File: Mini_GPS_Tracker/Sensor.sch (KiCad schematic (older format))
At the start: 13 parts, among them U2 MS5611-01BA, U7 LSM9DS1

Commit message: added stm chip
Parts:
- gave numbers to parts that had none: 5
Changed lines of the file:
@@
 $EndComp
 $Comp
-L Sensor_Motion:BNO055 U?
+L Sensor_Motion:BNO055 U12
 U 1 1 5E8555C8
 P 8300 4850
-F 0 "U?" H 8300 5731 50  0000 C CNN
+F 0 "U12" H 8300 5731 50  0000 C CNN
 F 1 "BNO055" H 8300 5640 50  0000 C CNN
 F 2 "Package_LGA:LGA-28_5.2x3.8mm_P0.5mm" H 8550 4200 50  0001 L CNN
@@
 $EndComp
 $Comp
-L Sensor_Motion:ADXL343 U?
+L Sensor_Motion:ADXL343 U11
 U 1 1 5E8940BD
 P 5450 2300
-F 0 "U?" H 5994 2346 50  0000 L CNN
+F 0 "U11" H 5994 2346 50  0000 L CNN
 F 1 "ADXL343" H 5994 2255 50  0000 L CNN
 F 2 "Package_LGA:LGA-14_3x5mm_P0.8mm_LayoutBorder1x6y" H 5450 2300 50  0001 C CNN
@@
 $EndComp
 $Comp
-L power:GND #PWR?
+L power:GND #PWR0119
 U 1 1 5E8951BC
 P 5450 3300
-F 0 "#PWR?" H 5450 3050 50  0001 C CNN
+F 0 "#PWR0119" H 5450 3050 50  0001 C CNN
 F 1 "GND" H 5455 3127 50  0000 C CNN
 F 2 "" H 5450 3300 50  0001 C CNN
@@
 	4400 2200 4950 2200
 $Comp
-L pspice:CAP C?
+L pspice:CAP C21
 U 1 1 5E89F2A3
 P 6650 2300
-F 0 "C?" H 6828 2346 50  0000 L CNN
+F 0 "C21" H 6828 2346 50  0000 L CNN
 F 1 "0.1uF" H 6828 2255 50  0000 L CNN
 F 2 "" H 6650 2300 50  0001 C CNN
@@
 $EndComp
 $Comp
-L pspice:CAP C?
+L pspice:CAP C22
 U 1 1 5E89F917
 P 7150 2300
-F 0 "C?" H 7328 2346 50  0000 L CNN
+F 0 "C22" H 7328 2346 50  0000 L CNN
 F 1 "0.1uF" H 7328 2255 50  0000 L CNN
 F 2 "" H 7150 2300 50  0001 C CNN
@@
 	5450 2900 5450 3150
 $Comp
-L pspice:CAP C?
+L pspice:CAP C23
 U 1 1 5E8A3F23
 P 7650 2300
-F 0 "C?" H 7828 2346 50  0000 L CNN
+F 0 "C23" H 7828 2346 50  0000 L CNN
 F 1 "10uF" H 7828 2255 50  0000 L CNN
 F 2 "" H 7650 2300 50  0001 C CNN

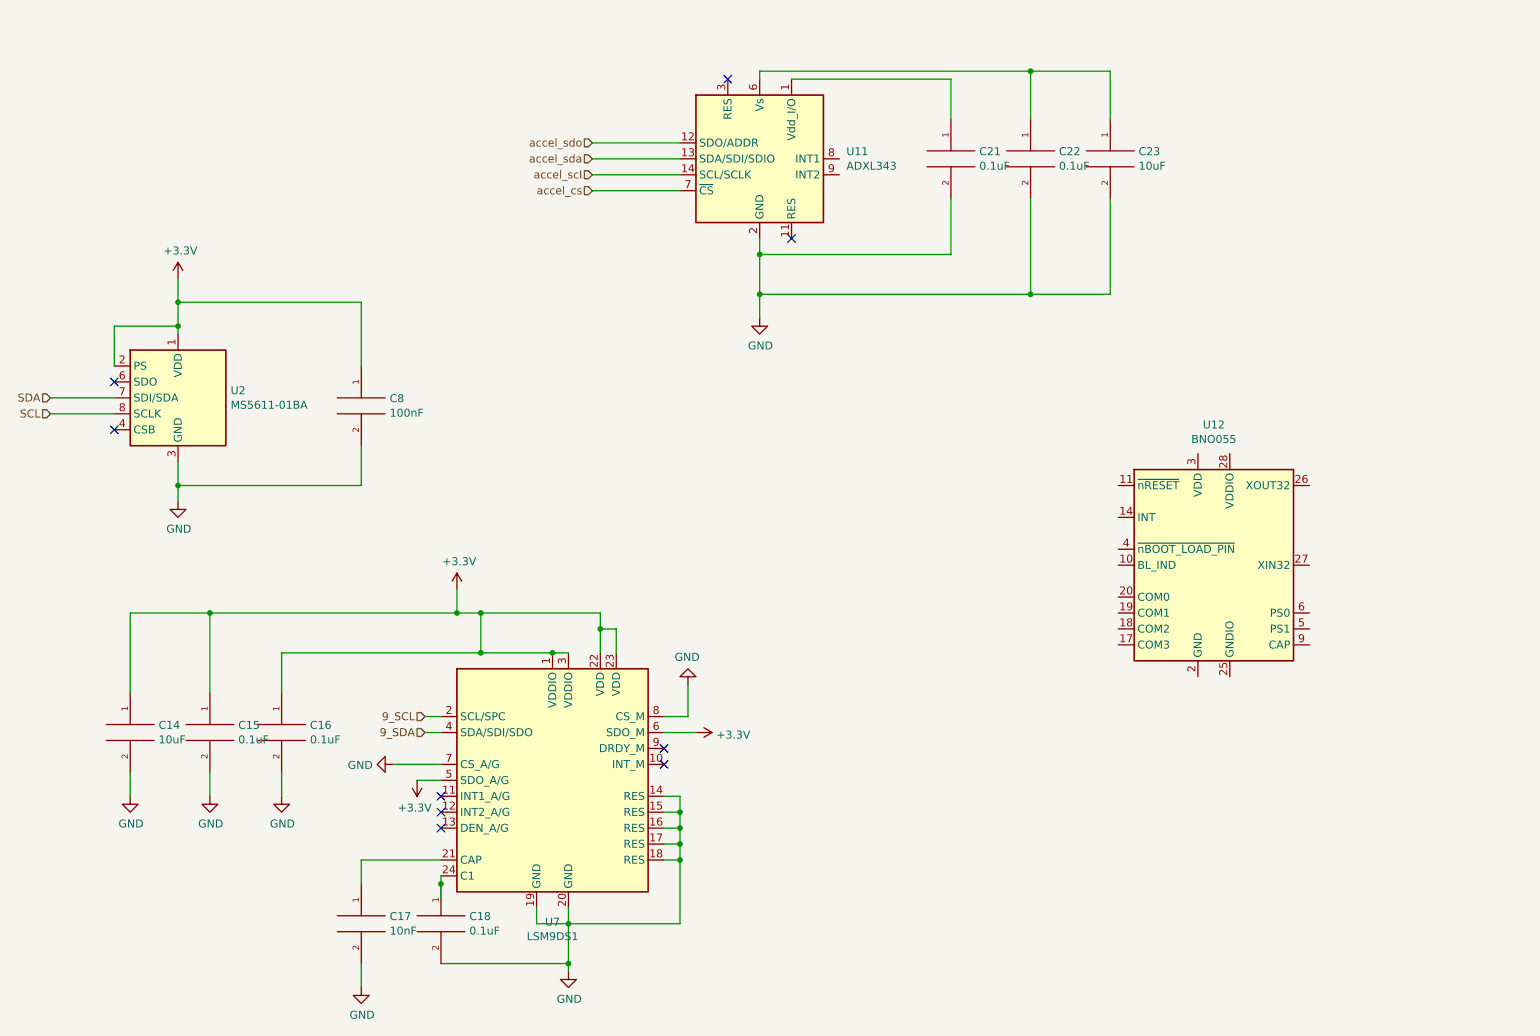
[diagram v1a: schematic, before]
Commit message: added bluetooth wifi module
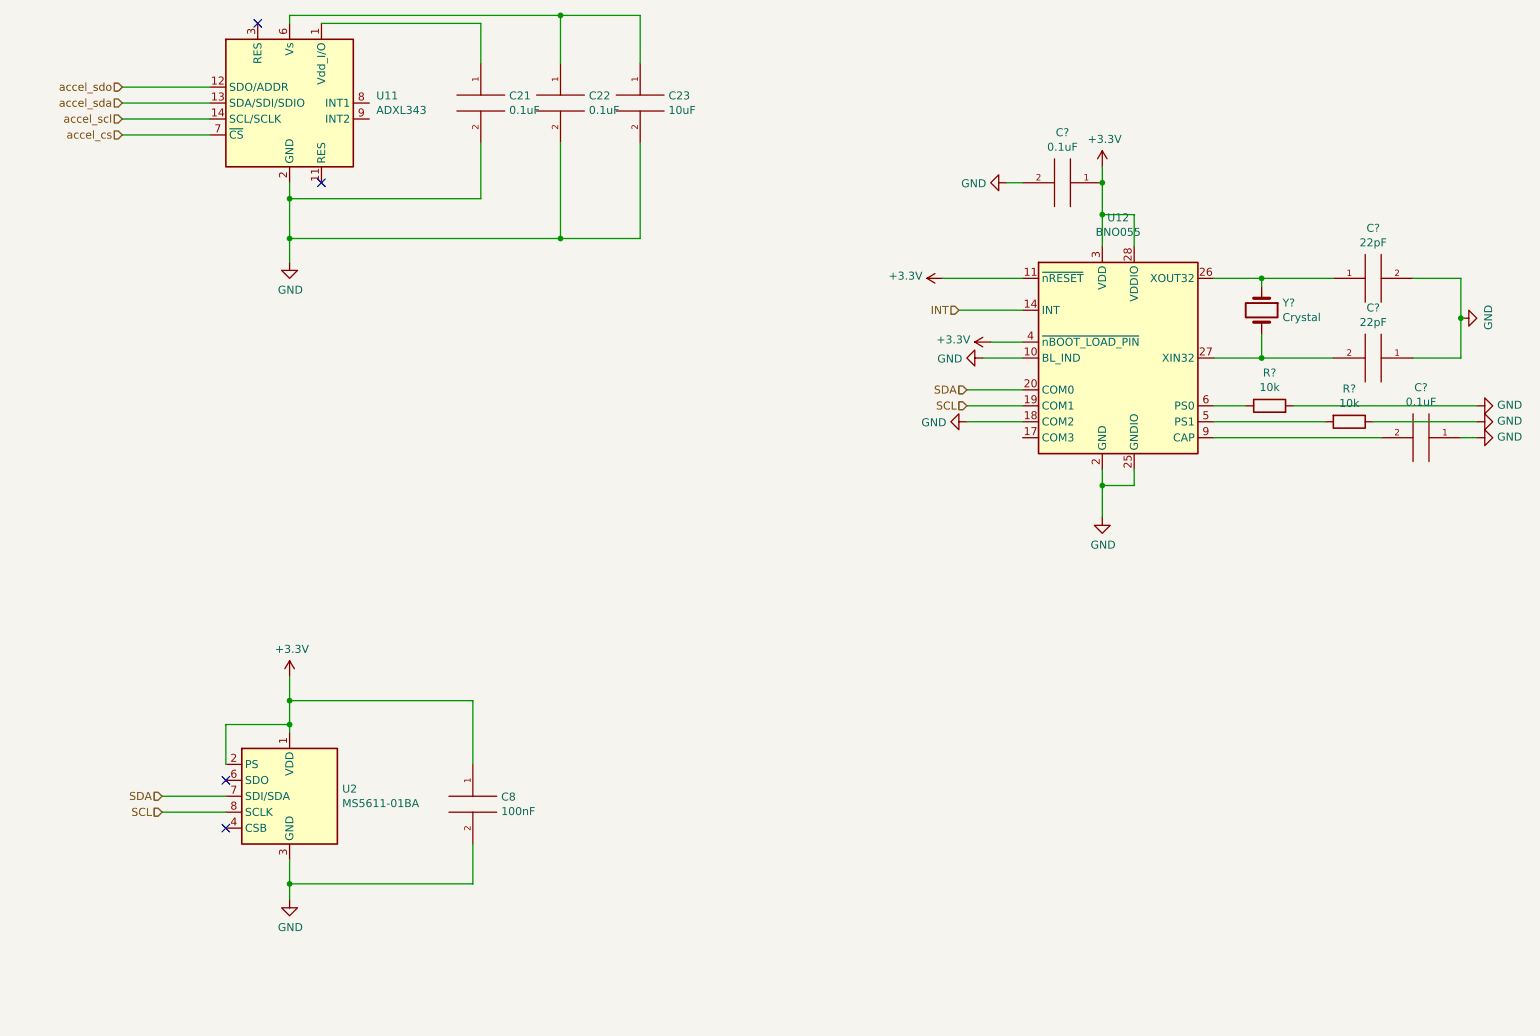
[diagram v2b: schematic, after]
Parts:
- removed C14: 10uF, Capacitor_SMD:C_0805_2012Metric_Pad1.15x1.40mm_HandSolder, symbol pspice:CAP
- removed C15, C16, C18: 0.1uF, Capacitor_SMD:C_0805_2012Metric_Pad1.15x1.40mm_HandSolder, symbol pspice:CAP
- removed C17: 10nF, Capacitor_SMD:C_0805_2012Metric_Pad1.15x1.40mm_HandSolder, symbol pspice:CAP
- removed U7: LSM9DS1, Package_LGA:LGA-24L_3x3.5mm_P0.43mm, symbol Sensor_Motion:LSM9DS1
- added C? (x2): 22pF, symbol pspice:CAP
- added C? (x2): 0.1uF, symbol pspice:CAP
- added R? (x2): 10k, symbol Device:R
- added Y?: Crystal, symbol Device:Crystal
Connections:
- net +3V3: now also U12.11 (~nRESET), U12.28 (VDDIO), U12.3 (VDD), U12.4 (~nBOOT_LOAD_PIN), C?.1
- net GND: now also U12.10 (BL_IND), U12.15 (GNDIO), U12.16 (GNDIO), U12.18 (COM2), U12.2 (GND), U12.25 (GNDIO), C?.1, C?.1, C?.2, C?.2, R?.1, R?.2
- net SCL: now also U12.19 (COM1)
- net SDA: now also U12.20 (COM0)
- net INT: now reaches U12.14 (INT)
- net at U12.26 (XOUT32): now also C?.1, Y?.1
- net at U12.27 (XIN32): now also C?.2, Y?.2
- net at U12.5 (PS1): now also R?.2
- net at U12.6 (PS0): now also R?.1
- net at U12.9 (CAP): now also C?.2
- no-connect marks 9 -> 4
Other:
- moved on the sheet: C21, C22, C23, C8, U11, U12, U2

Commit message: added motion
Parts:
- added R?: 10K, symbol Device:R
- Y?: value Crystal -> 32.7568KHz
- renumbered C8 to C?, C21 to C?, C22 to C?, C23 to C?, U2 to U?, U12 to U?, U11 to U?
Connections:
- net +3V3: no longer U?.11 (~nRESET)
- net GND: now also C?.2, R?.2; no longer C?.1
- net SCL: no longer U?.19 (COM1)
- net SDA: no longer U?.20 (COM0)
- net at U?.17 (COM3): now also R?.1
- net at U?.9 (CAP): now also C?.1; no longer C?.2
- net INT renamed BNO055_INTERRUPT
- new net BNO055_RESET: U?.11 (~nRESET)
- new net BNO055_SCL: U?.19 (COM1)
- new net BNO055_SDA: U?.20 (COM0)
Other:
- moved on the sheet: C?
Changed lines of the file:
@@
 $EndDescr
 $Comp
-L Sensor_Motion:BNO055 U12
+L Sensor_Motion:BNO055 U?
 U 1 1 5E8555C8
 P 7700 3550
-F 0 "U12" H 7700 4431 50  0000 C CNN
+F 0 "U?" H 7700 4431 50  0000 C CNN
 F 1 "BNO055" H 7700 4340 50  0000 C CNN
 F 2 "Package_LGA:LGA-28_5.2x3.8mm_P0.5mm" H 7950 2900 50  0001 L CNN
@@
 	2500 6700 2500 6850
 $Comp
-L pspice:CAP C8
+L pspice:CAP C?
 U 1 1 5E6E943F
 P 3650 6350
-F 0 "C8" H 3828 6396 50  0000 L CNN
+F 0 "C?" H 3828 6396 50  0000 L CNN
 F 1 "100nF" H 3828 6305 50  0000 L CNN
 F 2 "Capacitor_SMD:C_0805_2012Metric_Pad1.15x1.40mm_HandSolder" H 3650 6350 50  0001 C CNN
@@
 $EndComp
 $Comp
-L power:+3.3V #PWR016
+L power:+3.3V #PWR?
 U 1 1 5E6E8AC2
 P 2500 5550
-F 0 "#PWR016" H 2500 5400 50  0001 C CNN
+F 0 "#PWR?" H 2500 5400 50  0001 C CNN
 F 1 "+3.3V" H 2515 5723 50  0000 C CNN
 F 2 "" H 2500 5550 50  0001 C CNN
@@
 $EndComp
 $Comp
-L power:GND #PWR017
+L power:GND #PWR?
 U 1 1 5E6E7BFC
 P 2500 6950
-F 0 "#PWR017" H 2500 6700 50  0001 C CNN
+F 0 "#PWR?" H 2500 6700 50  0001 C CNN
 F 1 "GND" H 2505 6777 50  0000 C CNN
 F 2 "" H 2500 6950 50  0001 C CNN
@@
 	1700 6400 2100 6400
 $Comp
-L Sensor_Pressure:MS5611-01BA U2
+L Sensor_Pressure:MS5611-01BA U?
 U 1 1 5E6E6D79
 P 2500 6300
-F 0 "U2" H 2830 6346 50  0000 L CNN
+F 0 "U?" H 2830 6346 50  0000 L CNN
 F 1 "MS5611-01BA" H 2830 6255 50  0000 L CNN
 F 2 "Package_LGA:LGA-8_3x5mm_P1.25mm" H 2500 6300 50  0001 C CNN
@@
 $EndComp
 $Comp
-L Sensor_Motion:ADXL343 U11
+L Sensor_Motion:ADXL343 U?
 U 1 1 5E8940BD
 P 2500 1950
-F 0 "U11" H 3044 1996 50  0000 L CNN
+F 0 "U?" H 3044 1996 50  0000 L CNN
 F 1 "ADXL343" H 3044 1905 50  0000 L CNN
 F 2 "Package_LGA:LGA-14_3x5mm_P0.8mm_LayoutBorder1x6y" H 2500 1950 50  0001 C CNN
@@
 $EndComp
 $Comp
-L power:GND #PWR0119
+L power:GND #PWR?
 U 1 1 5E8951BC
 P 2500 2950
-F 0 "#PWR0119" H 2500 2700 50  0001 C CNN
+F 0 "#PWR?" H 2500 2700 50  0001 C CNN
 F 1 "GND" H 2505 2777 50  0000 C CNN
 F 2 "" H 2500 2950 50  0001 C CNN
@@
 	1450 1850 2000 1850
 $Comp
-L pspice:CAP C21
+L pspice:CAP C?
 U 1 1 5E89F2A3
 P 3700 1950
-F 0 "C21" H 3878 1996 50  0000 L CNN
+F 0 "C?" H 3878 1996 50  0000 L CNN
 F 1 "0.1uF" H 3878 1905 50  0000 L CNN
 F 2 "" H 3700 1950 50  0001 C CNN
@@
 $EndComp
 $Comp
-L pspice:CAP C22
+L pspice:CAP C?
 U 1 1 5E89F917
 P 4200 1950
-F 0 "C22" H 4378 1996 50  0000 L CNN
+F 0 "C?" H 4378 1996 50  0000 L CNN
 F 1 "0.1uF" H 4378 1905 50  0000 L CNN
 F 2 "" H 4200 1950 50  0001 C CNN
@@
 	2500 2550 2500 2800
 $Comp
-L pspice:CAP C23
+L pspice:CAP C?
 U 1 1 5E8A3F23
 P 4700 1950
-F 0 "C23" H 4878 1996 50  0000 L CNN
+F 0 "C?" H 4878 1996 50  0000 L CNN
 F 1 "10uF" H 4878 1905 50  0000 L CNN
 F 2 "" H 4700 1950 50  0001 C CNN
@@
 P 8600 3250
 F 0 "Y?" V 8554 3381 50  0000 L CNN
-F 1 "Crystal" V 8645 3381 50  0000 L CNN
+F 1 "32.7568KHz" V 8645 3381 50  0000 L CNN
 F 2 "" H 8600 3250 50  0001 C CNN
 F 3 "~" H 8600 3250 50  0001 C CNN
@@
 Wire Wire Line
 	8600 3050 9050 3050
-$Comp
-L power:+3.3V #PWR?
-U 1 1 5E88C4D2
-P 6900 3450
-F 0 "#PWR?" H 6900 3300 50  0001 C CNN
-F 1 "+3.3V" V 6915 3578 50  0000 L CNN
-F 2 "" H 6900 3450 50  0001 C CNN
-F 3 "" H 6900 3450 50  0001 C CNN
-	1    6900 3450
-	0    -1   -1   0
-$EndComp
-Wire Wire Line
-	6900 3450 7100 3450
 $Comp
 L power:GND #PWR?
@@
 L pspice:CAP C?
 U 1 1 5E8959B0
-P 9600 4050
-F 0 "C?" V 9285 4050 50  0000 C CNN
-F 1 "0.1uF" V 9376 4050 50  0000 C CNN
-F 2 "" H 9600 4050 50  0001 C CNN
-F 3 "~" H 9600 4050 50  0001 C CNN
-	1    9600 4050
-	0    1    1    0
+P 8550 4450
+F 0 "C?" V 8235 4450 50  0000 C CNN
+F 1 "0.1uF" V 8326 4450 50  0000 C CNN
+F 2 "" H 8550 4450 50  0001 C CNN
+F 3 "~" H 8550 4450 50  0001 C CNN
+	1    8550 4450
+	1    0    0    -1
 $EndComp
 $Comp
 L power:GND #PWR?
 U 1 1 5E89C6D8
-P 9950 4050
-F 0 "#PWR?" H 9950 3800 50  0001 C CNN
-F 1 "GND" V 9955 3922 50  0000 R CNN
-F 2 "" H 9950 4050 50  0001 C CNN
-F 3 "" H 9950 4050 50  0001 C CNN
-	1    9950 4050
-	0    -1   -1   0
+P 8550 4800
+F 0 "#PWR?" H 8550 4550 50  0001 C CNN
+F 1 "GND" V 8555 4672 50  0000 R CNN
+F 2 "" H 8550 4800 50  0001 C CNN
+F 3 "" H 8550 4800 50  0001 C CNN
+	1    8550 4800
+	1    0    0    -1
 $EndComp
 Wire Wire Line
@@
 	8300 3950 9000 3950
 Wire Wire Line
-	8300 4050 9350 4050
-Wire Wire Line
-	9850 4050 9950 4050
+	8550 4700 8550 4800
 Wire Wire Line
 	9300 3950 9950 3950
-$Comp
-L power:+3.3V #PWR?
-U 1 1 5E8A2C38
-P 6600 3050
-F 0 "#PWR?" H 6600 2900 50  0001 C CNN
-F 1 "+3.3V" V 6615 3178 50  0000 L CNN
-F 2 "" H 6600 3050 50  0001 C CNN
-F 3 "" H 6600 3050 50  0001 C CNN
-	1    6600 3050
-	0    -1   -1   0
-$EndComp
-Wire Wire Line
-	6600 3050 7100 3050
-Text HLabel 6750 3750 0    50   Input ~ 0
-SDA
-Text HLabel 6750 3850 0    50   Input ~ 0
-SCL
-Wire Wire Line
-	6750 3750 7100 3750
-Wire Wire Line
-	6750 3850 7100 3850
-$Comp
-L power:GND #PWR?
-U 1 1 5E8A7FB3
-P 6750 3950
-F 0 "#PWR?" H 6750 3700 50  0001 C CNN
-F 1 "GND" V 6755 3822 50  0000 R CNN
-F 2 "" H 6750 3950 50  0001 C CNN
-F 3 "" H 6750 3950 50  0001 C CNN
-	1    6750 3950
-	0    1    1    0
-$EndComp
-Wire Wire Line
-	6750 3950 7100 3950
 Wire Wire Line
 	7800 4250 7800 4350
@@
 Wire Wire Line
 	7600 4350 7600 4550
-$Comp
-L power:GND #PWR?
-U 1 1 5E8AC9F0
-P 6850 3550
-F 0 "#PWR?" H 6850 3300 50  0001 C CNN
-F 1 "GND" V 6855 3422 50  0000 R CNN
-F 2 "" H 6850 3550 50  0001 C CNN
-F 3 "" H 6850 3550 50  0001 C CNN
-	1    6850 3550
-	0    1    1    0
-$EndComp
-Wire Wire Line
-	6850 3550 7100 3550
-Text HLabel 6700 3250 0    50   Input ~ 0
-INT
-Wire Wire Line
-	6700 3250 7100 3250
+Wire Wire Line
+	8300 4050 8550 4050
+Wire Wire Line
+	8550 4050 8550 4200
+$Comp
+L Device:R R?
+U 1 1 5E897EFC
+P 6950 4300
+F 0 "R?" H 7020 4346 50  0000 L CNN
+F 1 "10K" H 7020 4255 50  0000 L CNN
+F 2 "" V 6880 4300 50  0001 C CNN
+F 3 "~" H 6950 4300 50  0001 C CNN
+	1    6950 4300
+	1    0    0    -1
+$EndComp
+$Comp
+L power:GND #PWR?
+U 1 1 5E898E99
+P 6950 4550
+F 0 "#PWR?" H 6950 4300 50  0001 C CNN
+F 1 "GND" H 6955 4377 50  0000 C CNN
+F 2 "" H 6950 4550 50  0001 C CNN
+F 3 "" H 6950 4550 50  0001 C CNN
+	1    6950 4550
+	1    0    0    -1
+$EndComp
+$Comp
+L power:GND #PWR?
+U 1 1 5E89968D
+P 6600 4550
+F 0 "#PWR?" H 6600 4300 50  0001 C CNN
+F 1 "GND" H 6605 4377 50  0000 C CNN
+F 2 "" H 6600 4550 50  0001 C CNN
+F 3 "" H 6600 4550 50  0001 C CNN
+	1    6600 4550
+	1    0    0    -1
+$EndComp
+Wire Wire Line
+	6950 4550 6950 4450
+Wire Wire Line
+	6950 4150 6950 4050
+Wire Wire Line
+	6950 4050 7100 4050
+Wire Wire Line
+	7100 3950 6600 3950
+Wire Wire Line
+	6600 3950 6600 4550
+Text HLabel 6550 3850 0    50   Input ~ 0
+BNO055_SCL
+Text HLabel 6550 3750 0    50   Input ~ 0
+BNO055_SDA
+Text HLabel 6500 3050 0    50   Input ~ 0
+BNO055_RESET
+Text HLabel 6500 3250 0    50   Input ~ 0
+BNO055_INTERRUPT
+Wire Wire Line
+	6500 3050 7100 3050
+Wire Wire Line
+	6500 3250 7100 3250
+Wire Wire Line
+	6550 3750 7100 3750
+Wire Wire Line
+	6550 3850 7100 3850
+$Comp
+L power:GND #PWR?
+U 1 1 5E8A27A4
+P 5500 3550
+F 0 "#PWR?" H 5500 3300 50  0001 C CNN
+F 1 "GND" H 5505 3377 50  0000 C CNN
+F 2 "" H 5500 3550 50  0001 C CNN
+F 3 "" H 5500 3550 50  0001 C CNN
+	1    5500 3550
+	1    0    0    -1
+$EndComp
+$Comp
+L power:+3.3V #PWR?
+U 1 1 5E8A32E9
+P 5500 3450
+F 0 "#PWR?" H 5500 3300 50  0001 C CNN
+F 1 "+3.3V" H 5515 3623 50  0000 C CNN
+F 2 "" H 5500 3450 50  0001 C CNN
+F 3 "" H 5500 3450 50  0001 C CNN
+	1    5500 3450
+	1    0    0    -1
+$EndComp
+Wire Wire Line
+	5500 3450 7100 3450
+Wire Wire Line
+	7100 3550 5500 3550
 $EndSCHEMATC
